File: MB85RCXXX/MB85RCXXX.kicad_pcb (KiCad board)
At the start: 2 copper layers, 18 x 16.8 mm, 17 parts, among them J1 Conn_01x05

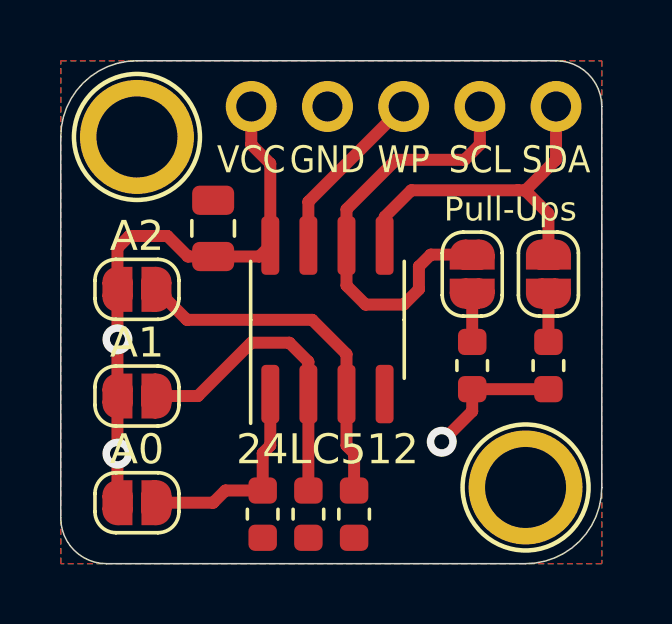
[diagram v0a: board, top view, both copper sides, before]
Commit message: MB85RXXX Added in place of MB85RC256V
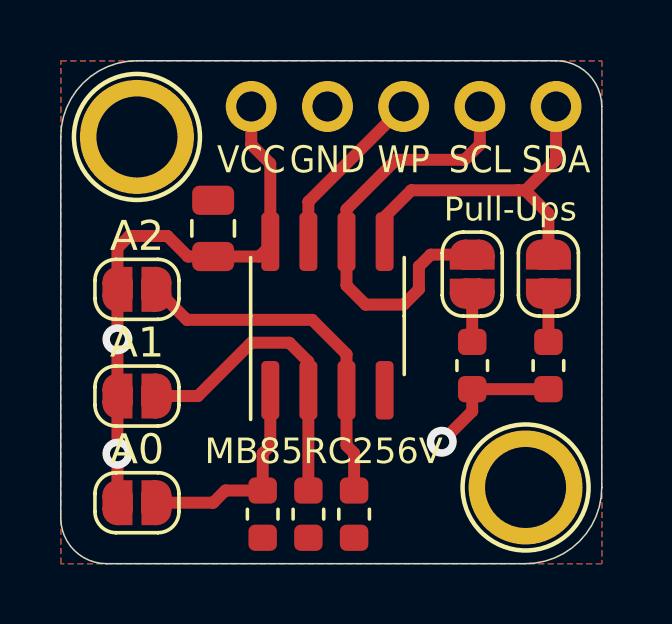
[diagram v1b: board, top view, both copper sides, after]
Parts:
- removed 24LC512: 24LC1025, Package_SO:SOIC-8_3.9x4.9mm_P1.27mm
- added MB85RC256V: MB85RC256V, Package_SO:SOIC-8_3.9x4.9mm_P1.27mm, F.Cu at (58.4, 42.5)
- C1: value 1uF -> 10uF
- G***: footprint logo:logo76x107 -> logo:logo63x89
- J1: moved to B.Cu
- moved G*** 2.17 mm to (59.1, 46.6)
- moved G*** 0.38 mm to (53.5, 44.8)
- turned J1 to 270 degrees
- renumbered SCL to SCL1, SDA to SDA1
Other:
- board text added: "128kB"
- board text added: "16kB"
- board text added: "32kB"
- board text added: "64kB"
- board text added: "8kB"
- board text added: "MB85RCXXX I2C FRAM"
- board text removed: "24LC512 Board I2C EEPROM 64kBytes"
